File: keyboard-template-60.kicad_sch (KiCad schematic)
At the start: 175 parts, among them J1 USB_C_Receptacle_USB2.0, J2 Conn_01x04_MountingPin, J3 AVR-ISP-6, SW1 SW_Reset, U1 ATmega32U4-M, U2 SRV05-4, Y1 16MHz

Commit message: introduce trackpoint files and placement - VERY ROUGH WIP
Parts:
- added C9: 2.2uF, Capacitor_SMD:C_0603_1608Metric_Pad1.08x0.95mm_HandSolder, symbol Device:C_Small
- added R7, R8: 4.7K, Capacitor_SMD:C_0603_1608Metric_Pad1.08x0.95mm_HandSolder, symbol Device:R_Small
- added R9: 100K, Capacitor_SMD:C_0603_1608Metric_Pad1.08x0.95mm_HandSolder, symbol Device:R_Small
- added U3: TP_Sprintek_SK8707-01_Sensor, ssbb_parts:TP_Sprintek_SK8707-01_Sensor_reversible, symbol ssbb_parts:TP_Sprintek_SK8707-01_Sensor
- added U4: SK8707-01, ssbb_parts:TP_Sprintek_SK8707-01_reversible, symbol ssbb_parts:TP_Sprintek_SK8707–01
- H1, H2, H3, H4, H5, H6: footprint MountingHole:MountingHole_2.2mm_M2_Pad_TopOnly -> MountingHole:MountingHole_2.5mm
- J2: symbol Connector_Generic_MountingPin:Conn_01x04_MountingPin -> Connector_Generic:Conn_01x04
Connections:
- net COL1: now also U1.39 (PF4); no longer J3.1 (MISO), U1.11 (PB3)
- net COL3: now also U1.8 (PB0); no longer U1.22 (PD5)
- net COL5: now also U1.18 (PD0); no longer U1.20 (PD2)
- net GND: now also R9.2, U4.1 (GND)
- net ROW0: now also U1.41 (PF0); no longer U1.8 (PB0)
- net ROW1: now also U1.40 (PF1); no longer J3.3 (SCK), U1.9 (PB1)
- net VCC: now also C9.1, R7.2, R8.2, U4.5 (VCC)
- new net: C9.2, R9.1, U4.4 (RST)
- new net D2: R8.1, U1.20 (PD2), U4.2 (DATA)
- new net D5: R7.1, U1.22 (PD5), U4.3 (CLK)
- new net MISO: J3.1 (MISO), U1.11 (PB3)
- new net SCK: J3.3 (SCK), U1.9 (PB1)
- new net S_GND: U3.2 (S_GND), U4.10 (S_GND)
- new net S_VCC: U3.1 (S_VCC), U4.9 (S_VCC)
- new net S_X: U3.4 (S_X), U4.12 (S_X)
- new net S_Y: U3.3 (S_Y), U4.11 (S_Y)
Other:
- moved on the sheet: C1, C2, C3, C4, C5, C6, C7, C8, F1, J1, J3, R1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

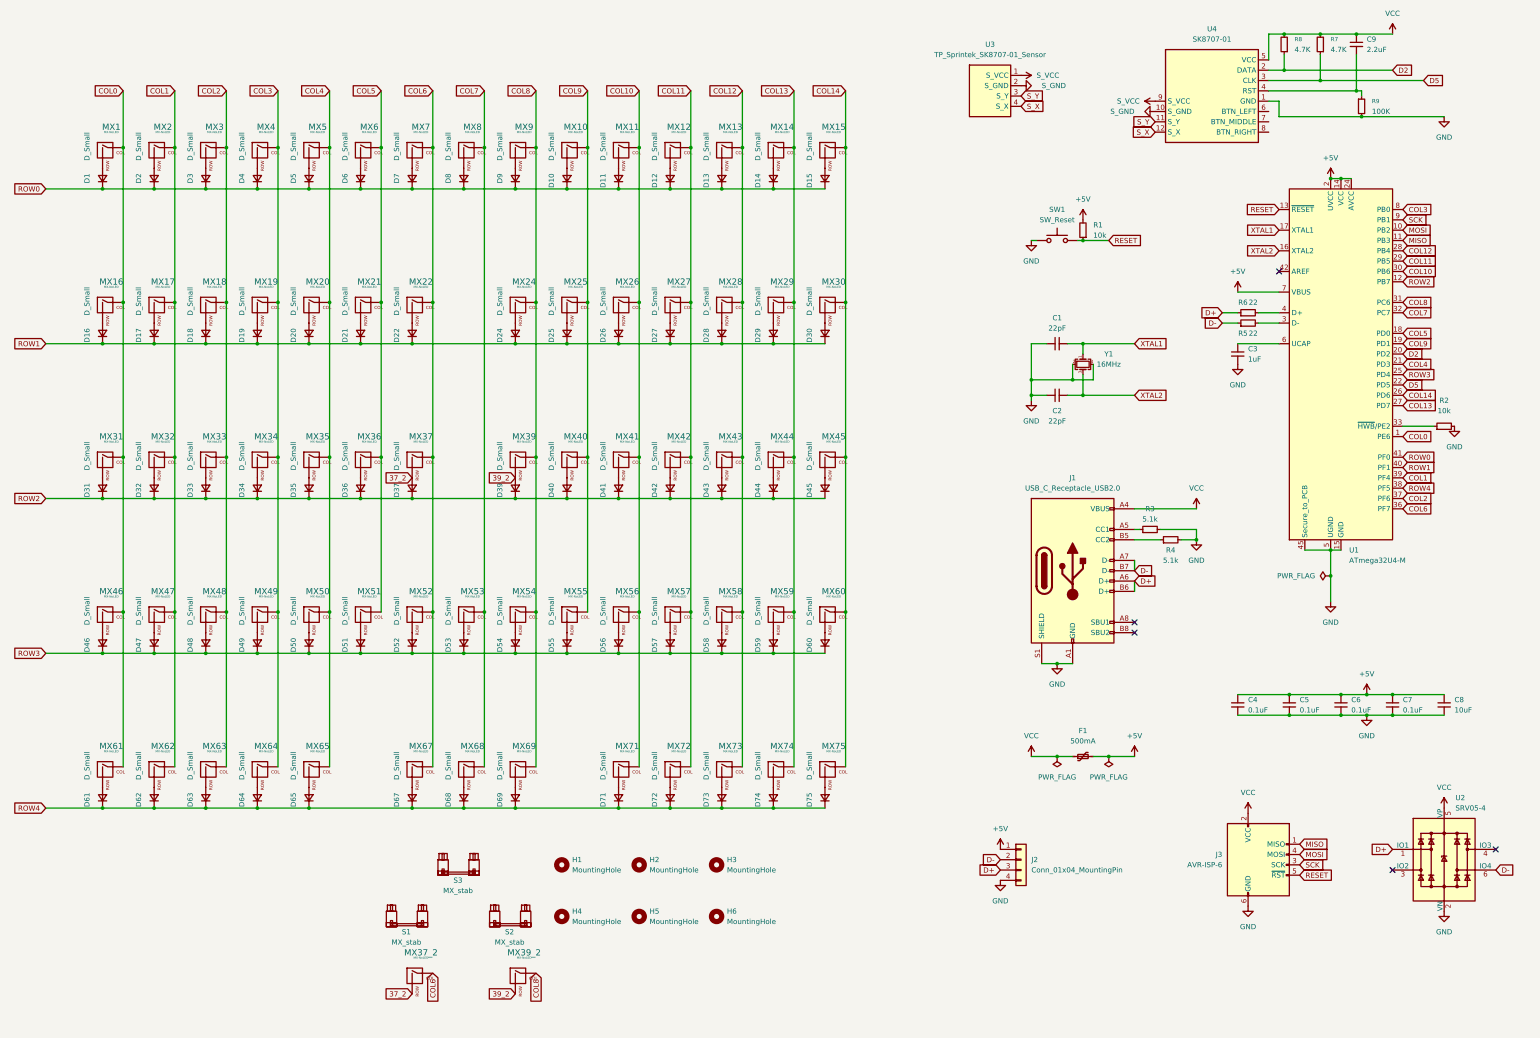
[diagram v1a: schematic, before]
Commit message: Integration of trackpoint, regulator and shifter
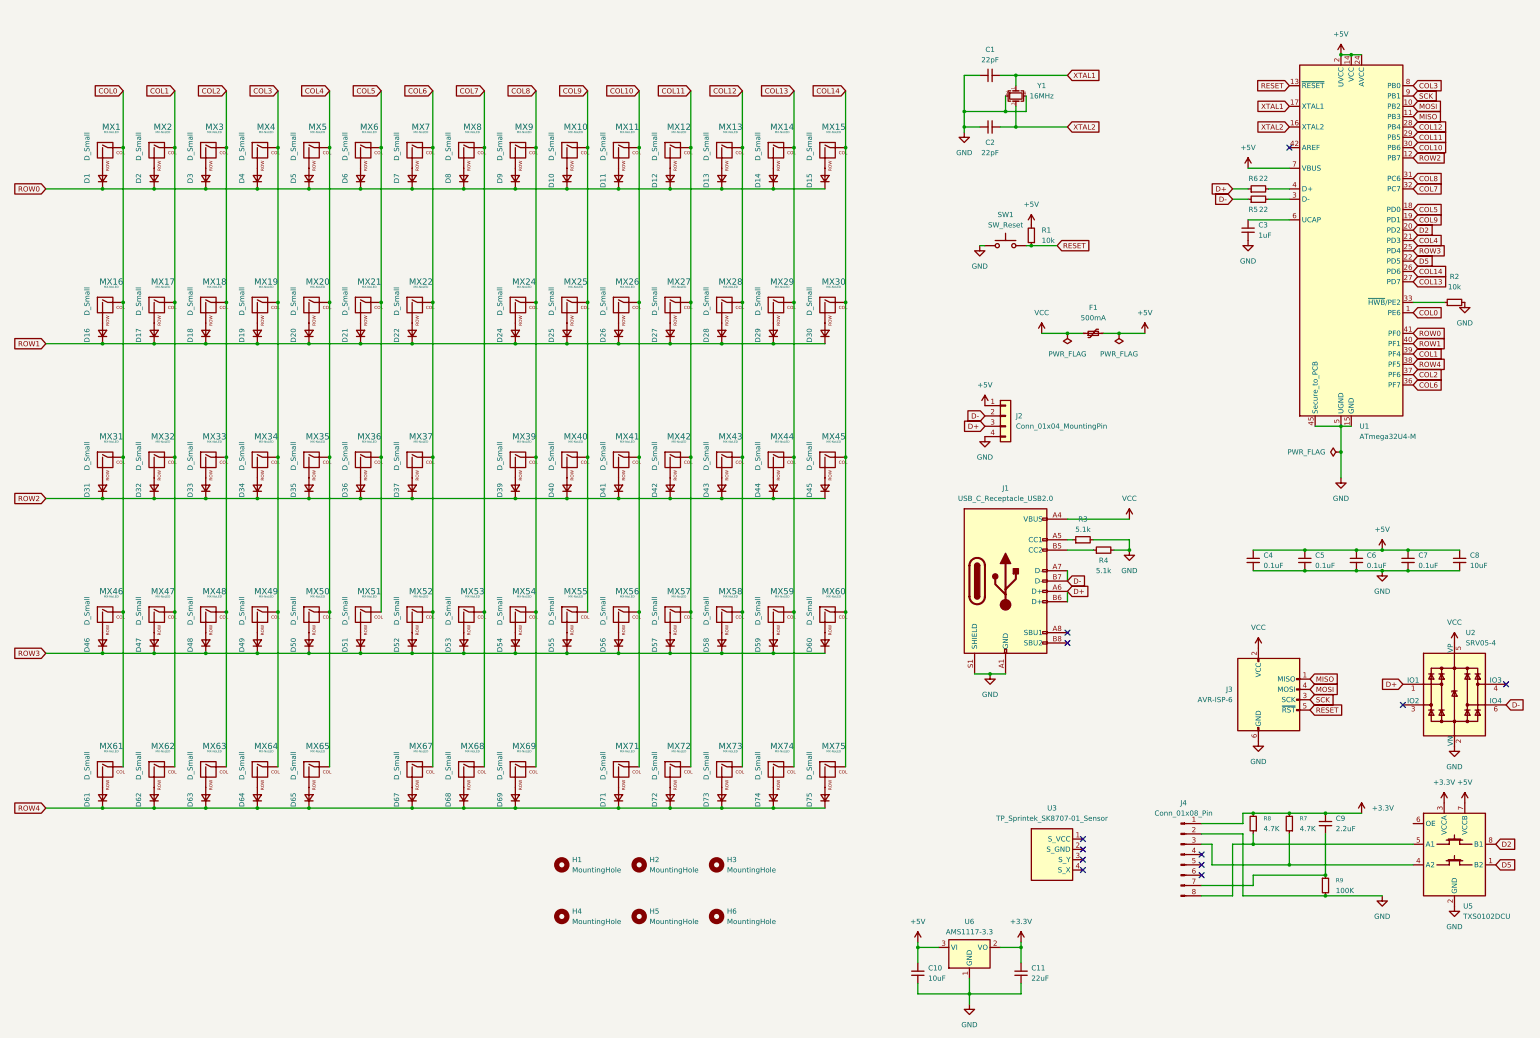
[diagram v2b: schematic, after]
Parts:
- removed MX37_2, MX39_2: MX-NoLED, marbastlib-mx:SW_MX_HS_1.25u, symbol MX_Alps_Hybrid:MX-NoLED
- removed S1, S2: MX_stab, marbastlib-mx:STAB_MX_2u, symbol marbastlib-mx:MX_stab
- removed S3: MX_stab, marbastlib-mx:STAB_MX_7u, symbol marbastlib-mx:MX_stab
- removed U4: SK8707-01, ssbb_parts:TP_Sprintek_SK8707-01_reversible, symbol ssbb_parts:TP_Sprintek_SK8707–01
- added C10: 10uF, Capacitor_SMD:C_0603_1608Metric_Pad1.08x0.95mm_HandSolder, symbol Device:C_Small
- added C11: 22uF, Capacitor_SMD:C_0603_1608Metric_Pad1.08x0.95mm_HandSolder, symbol Device:C_Small
- added J4: Conn_01x08_Pin, Connector_FFC-FPC:TE_84952-8_1x08-1MP_P1.0mm_Horizontal, symbol Connector:Conn_01x08_Pin
- added U5: TXS0102DCU, Package_SO:VSSOP-8_2.3x2mm_P0.5mm, symbol Logic_LevelTranslator:TXS0102DCU
- added U6: AMS1117-3.3, Package_TO_SOT_SMD:SOT-223-3_TabPin2, symbol Regulator_Linear:AMS1117-3.3
- MX1, MX10, MX11, MX12, MX13, MX14, MX15, MX17, MX18, MX19, MX2, MX20, MX21, MX22, MX24, MX25, MX26, MX27, MX28, MX29, MX3, MX32, MX33, MX34, MX35, MX36, MX37, MX39, MX4, MX40, MX41, MX42, MX43, MX44, MX46, MX47, MX48, MX49, MX5, MX50, MX51, MX52, MX53, MX54, MX55, MX56, MX57, MX58, MX59, MX6, MX60, MX61, MX62, MX63, MX64, MX65, MX7, MX71, MX72, MX73, MX74, MX75, MX8, MX9: footprint marbastlib-mx:SW_MX_HS_1u -> MX_Only:MXOnly-1U-Hotswap-Antishear
- MX16, MX30: footprint marbastlib-mx:SW_MX_HS_1.5u -> MX_Only:MXOnly-1U-Hotswap-Antishear
- MX31, MX45: footprint marbastlib-mx:SW_MX_HS_1.25u -> MX_Only:MXOnly-1U-Hotswap-Antishear
- MX67, MX69: footprint marbastlib-mx:SW_MX_HS_1u -> MX_Only:MXOnly-2U-Hotswap-ReversedStabilizers
- MX68: footprint marbastlib-mx:SW_MX_HS_1u -> MX_Only:MXOnly-7U-Hotswap
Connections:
- net +5V: now also C10.2, U5.7 (VCCB), U6.3 (VI)
- net D2: now also U5.8 (B1); no longer R8.1
- net D5: now also U5.1 (B2); no longer R7.1
- net GND: now also C10.1, C11.1, J4.2 (Pin_2), U5.2 (GND), U6.1 (GND)
- net VCC: no longer C9.1, R7.2, R8.2
- net at C9.2, R9.1: now also J4.7 (Pin_7)
- net 37_2: no longer names the net of D37.2 (A), MX37.2 (ROW)
- net 39_2: no longer names the net of D39.2 (A), MX39.2 (ROW)
- net S_GND: no longer names the net of U3.2 (S_GND)
- net S_VCC: no longer names the net of U3.1 (S_VCC)
- net S_X: no longer names the net of U3.4 (S_X)
- net S_Y: no longer names the net of U3.3 (S_Y)
- new net: J4.3 (Pin_3), R7.1, U5.4 (A2)
- new net: J4.8 (Pin_8), R8.1, U5.5 (A1)
- new net +3.3V: C11.2, C9.1, J4.1 (Pin_1), R7.2, R8.2, U5.3 (VCCA), U6.2 (VO)
- no-connect marks 5 -> 12
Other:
- moved on the sheet: C1, C2, C3, C4, C5, C6, C7, C8, C9, F1, J1, J2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

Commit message: Tracing of the new schematic layout
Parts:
- removed U5: TXS0102DCU, Package_SO:VSSOP-8_2.3x2mm_P0.5mm, symbol Logic_LevelTranslator:TXS0102DCU
- MX1, MX10, MX11, MX12, MX13, MX14, MX15, MX16, MX17, MX18, MX19, MX2, MX20, MX21, MX22, MX24, MX25, MX26, MX27, MX28, MX29, MX3, MX30, MX31, MX32, MX33, MX34, MX35, MX36, MX37, MX39, MX4, MX40, MX41, MX42, MX43, MX44, MX45, MX46, MX47, MX48, MX49, MX5, MX50, MX51, MX52, MX53, MX54, MX55, MX56, MX57, MX58, MX59, MX6, MX60, MX61, MX62, MX63, MX64, MX65, MX7, MX71, MX72, MX73, MX74, MX75, MX8, MX9: footprint MX_Only:MXOnly-1U-Hotswap-Antishear -> MX_Only:MXOnly-1U-Hotswap
- Y1: value 16MHz -> 8MHz
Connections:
- net +3.3V: now also C4.1, C5.1, C6.1, C7.1, C8.1, J2.1 (Pin_1), R1.2, U1.14 (VCC), U1.2 (UVCC), U1.24 (AVCC), U1.34 (VCC), U1.44 (AVCC), U1.7 (VBUS)
- net +5V: no longer C4.1, C5.1, C6.1, C7.1, C8.1, J2.1 (Pin_1), R1.2, U1.14 (VCC), U1.2 (UVCC), U1.24 (AVCC), U1.34 (VCC), U1.44 (AVCC), U1.7 (VBUS)
- net COL4: now also U1.36 (PF7); no longer U1.21 (PD3)
- net COL5: now also U1.38 (PF5); no longer U1.18 (PD0)
- net COL6: now also U1.21 (PD3); no longer U1.36 (PF7)
- net COL7: now also U1.19 (PD1); no longer U1.32 (PC7)
- net COL9: now also U1.32 (PC7); no longer U1.19 (PD1)
- net D+: no longer J2.3 (Pin_3), R6.1
- net D-: no longer J2.2 (Pin_2), R5.1
- net D2: now also J4.8 (Pin_8), R8.1
- net D5: now also J4.3 (Pin_3), R7.1
- net GND: no longer Y1.2, Y1.4
- net RESET: no longer R1.1, SW1.2, U1.13 (~{RESET})
- net ROW4: now also U1.18 (PD0); no longer U1.38 (PF5)
- net XTAL1: no longer names the net of C1.2, U1.17 (XTAL1), Y1.1
- net XTAL2: no longer names the net of C2.2, U1.16 (XTAL2), Y1.3
- new net: J2.2 (Pin_2), R5.1
- new net: J2.3 (Pin_3), R6.1
- new net: R1.1, SW1.2, U1.13 (~{RESET})
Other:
- moved on the sheet: C1, C10, C11, C2, C3, C4, C5, C6, C7, C8, C9, F1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

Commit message: More retracing
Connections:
- net COL6: now also U1.19 (PD1); no longer U1.21 (PD3)
- net COL7: now also U1.21 (PD3); no longer U1.19 (PD1)
- net GND: now also Y1.2, Y1.4
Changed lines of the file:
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@@
 	)
 	(junction
+		(at 321.31 52.07)
+		(diameter 0)
+		(color 0 0 0 0)
+	)
+	(junction
 		(at 179.07 62.23)
 		(diameter 0)
@@
 	(wire
 		(pts
+			(xy 321.31 54.61) (xy 332.74 54.61)
+		)
+		(stroke
+			(width 0)
+			(type default)
+		)
+	)
+	(wire
+		(pts
 			(xy 278.13 184.15) (xy 290.83 184.15)
 		)
@@
 	(wire
 		(pts
+			(xy 337.82 49.53) (xy 321.31 49.53)
+		)
+		(stroke
+			(width 0)
+			(type default)
+		)
+	)
+	(wire
+		(pts
 			(xy 52.07 100.33) (xy 64.77 100.33)
 		)
@@
 	(wire
 		(pts
+			(xy 321.31 49.53) (xy 321.31 52.07)
+		)
+		(stroke
+			(width 0)
+			(type default)
+		)
+	)
+	(wire
+		(pts
 			(xy 326.39 210.82) (xy 328.93 210.82)
 		)
@@
 	(wire
 		(pts
+			(xy 337.82 54.61) (xy 337.82 49.53)
+		)
+		(stroke
+			(width 0)
+			(type default)
+		)
+	)
+	(wire
+		(pts
 			(xy 107.95 166.37) (xy 107.95 204.47)
 		)
@@
 	(global_label "COL6"
 		(shape input)
-		(at 374.65 85.09 0)
+		(at 374.65 80.01 0)
 		(fields_autoplaced yes)
 		(effects
@@
 		)
 		(property "Intersheetrefs" "${INTERSHEET_REFS}"
-			(at 381.9012 85.1694 0)
+			(at 381.9012 80.0894 0)
 			(effects
 				(font
@@
 	(global_label "COL7"
 		(shape input)
-		(at 374.65 80.01 0)
+		(at 374.65 85.09 0)
 		(fields_autoplaced yes)
 		(effects
@@
 		)
 		(property "Intersheetrefs" "${INTERSHEET_REFS}"
-			(at 381.9012 80.0894 0)
+			(at 381.9012 85.1694 0)
 			(effects
 				(font

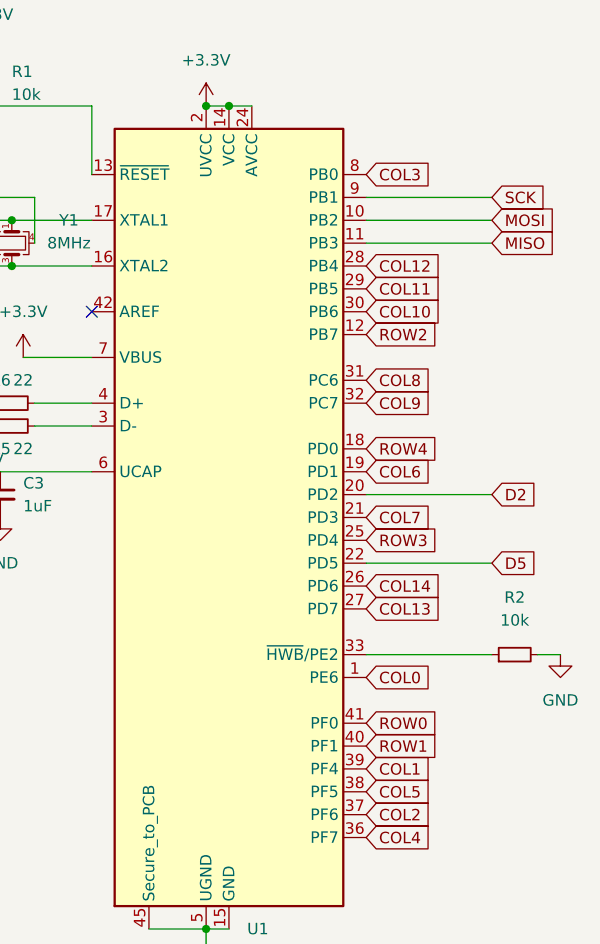
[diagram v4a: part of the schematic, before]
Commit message: updated traces, components
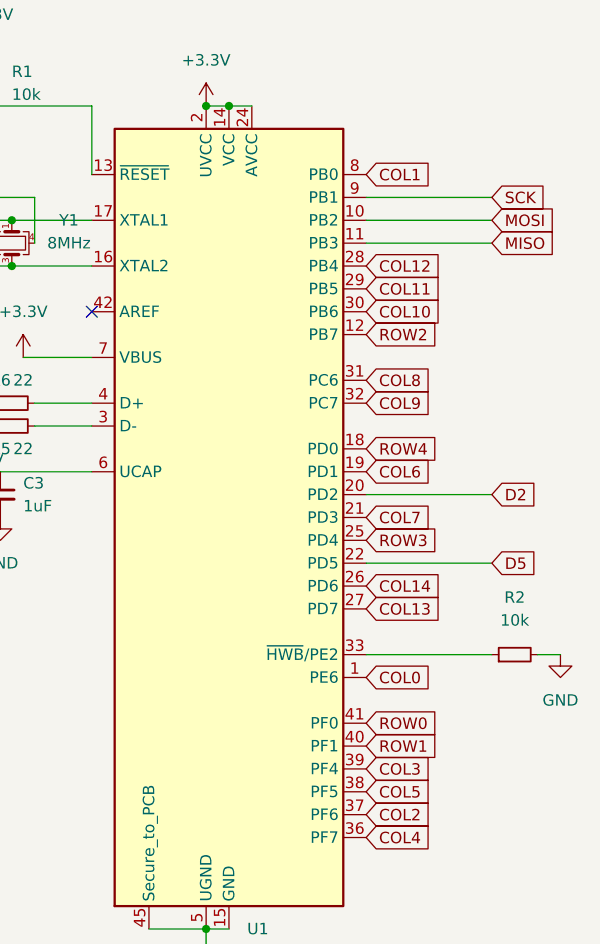
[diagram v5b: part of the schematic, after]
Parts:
- MX1, MX10, MX11, MX12, MX13, MX14, MX15, MX16, MX17, MX18, MX19, MX2, MX20, MX21, MX22, MX24, MX25, MX26, MX27, MX28, MX29, MX3, MX30, MX31, MX32, MX33, MX34, MX35, MX36, MX37, MX39, MX4, MX40, MX41, MX42, MX43, MX44, MX45, MX46, MX47, MX48, MX49, MX5, MX50, MX51, MX52, MX53, MX54, MX55, MX56, MX57, MX58, MX59, MX6, MX60, MX61, MX62, MX63, MX64, MX65, MX7, MX71, MX72, MX73, MX74, MX75, MX8, MX9: footprint MX_Only:MXOnly-1U-Hotswap -> PCM_marbastlib-mx:SW_MX_HS_CPG151101S11_1u
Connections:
- net COL1: now also U1.8 (PB0); no longer U1.39 (PF4)
- net COL3: now also U1.39 (PF4); no longer U1.8 (PB0)
